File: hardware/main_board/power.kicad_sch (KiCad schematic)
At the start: 29 parts, among them J1 USB_C_Receptacle_USB2.0_16P, J2 Conn_01x03, SW1 SW_Push, U1 USBLC6-2SC6, U2 BQ24259RGER, U3 TPS7A0533PDBV

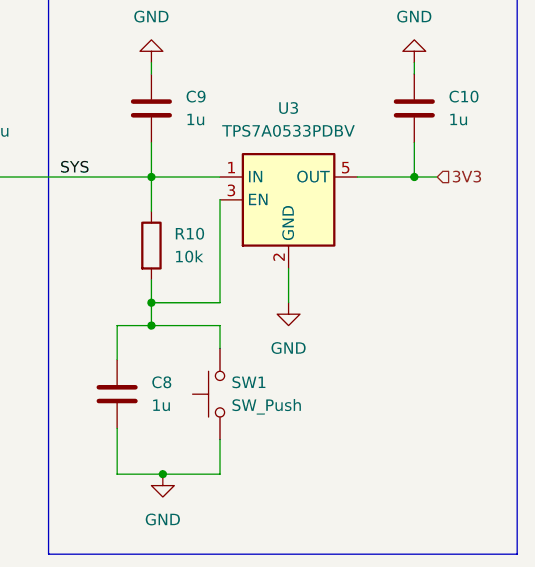
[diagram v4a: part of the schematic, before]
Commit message: Board schematic complete
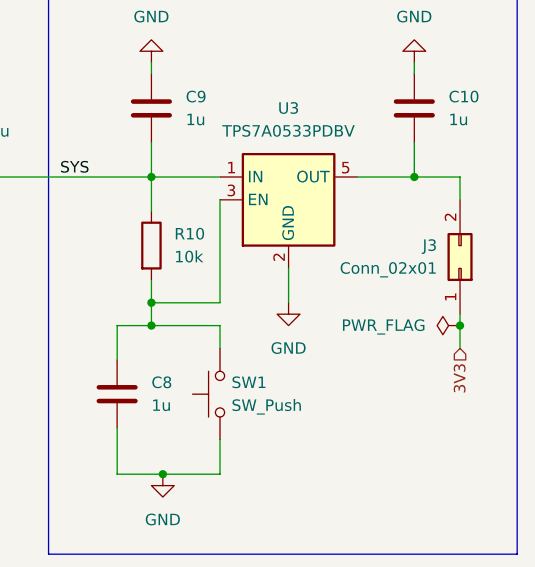
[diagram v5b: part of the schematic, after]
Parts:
- added J3: Conn_02x01, symbol Connector_Generic:Conn_02x01
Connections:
- net 3V3: now also J3.1 (Pin_1); no longer C10.2, U3.5 (OUT)
- new net: C10.2, J3.2 (Pin_2), U3.5 (OUT)
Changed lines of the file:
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@@
 	)
 	(junction
+		(at 273.05 111.76)
+		(diameter 0)
+		(color 0 0 0 0)
+	)
+	(junction
 		(at 240.03 128.27)
 		(diameter 0)
@@
 	(wire
 		(pts
-			(xy 267.97 95.25) (xy 270.51 95.25)
+			(xy 267.97 95.25) (xy 273.05 95.25)
 		)
 		(stroke
@@
 	(wire
 		(pts
+			(xy 273.05 110.49) (xy 273.05 111.76)
+		)
+		(stroke
+			(width 0)
+			(type default)
+		)
+	)
+	(wire
+		(pts
 			(xy 59.69 127) (xy 59.69 125.73)
 		)
@@
 	(wire
 		(pts
+			(xy 273.05 111.76) (xy 273.05 114.3)
+		)
+		(stroke
+			(width 0)
+			(type default)
+		)
+	)
+	(wire
+		(pts
 			(xy 59.69 90.17) (xy 74.93 90.17)
 		)
@@
 		)
 	)
+	(wire
+		(pts
+			(xy 273.05 95.25) (xy 273.05 97.79)
+		)
+		(stroke
+			(width 0)
+			(type default)
+		)
+	)
 	(rectangle
 		(start 227.33 71.12)
@@
 	(hierarchical_label "3V3"
 		(shape input)
-		(at 270.51 95.25 0)
+		(at 273.05 114.3 270)
 		(effects
 			(font
 				(size 1.27 1.27)
 			)
-			(justify left)
+			(justify right)
 		)
 	)
@@
 	)
 	(symbol
+		(lib_id "power:PWR_FLAG")
+		(at 273.05 111.76 90)
+		(unit 1)
+		(exclude_from_sim no)
+		(in_bom yes)
+		(on_board yes)
+		(dnp no)
+		(fields_autoplaced yes)
+		(property "Reference" "#FLG03"
+			(at 271.145 111.76 0)
+			(effects
+				(font
+					(size 1.27 1.27)
+				)
+				(hide yes)
+			)
+		)
+		(property "Value" "PWR_FLAG"
+			(at 269.24 111.7599 90)
+			(effects
+				(font
+					(size 1.27 1.27)
+				)
+				(justify left)
+			)
+		)
+		(property "Footprint" ""
+			(at 273.05 111.76 0)
+			(effects
+				(font
+					(size 1.27 1.27)
+				)
+				(hide yes)
+			)
+		)
+		(property "Datasheet" "~"
+			(at 273.05 111.76 0)
+			(effects
+				(font
+					(size 1.27 1.27)
+				)
+				(hide yes)
+			)
+		)
+		(property "Description" "Special symbol for telling ERC where power comes from"
+			(at 273.05 111.76 0)
+			(effects
+				(font
+					(size 1.27 1.27)
+				)
+				(hide yes)
+			)
+		)
+		(pin "1"
+		)
+		(instances
+			(project ""
+				(path "/e7586151-38a0-41a9-9cce-542cfb7665db/36d2f76b-6786-406f-96a1-52265f303dbc"
+					(reference "#FLG03")
+					(unit 1)
+				)
+			)
+		)
+	)
+	(symbol
 		(lib_id "Device:C")
 		(at 189.23 106.68 0)
@@
 					(unit 1)
 				)
+			)
+		)
+	)
+	(symbol
+		(lib_id "Connector_Generic:Conn_02x01")
+		(at 273.05 105.41 270)
+		(mirror x)
+		(unit 1)
+		(exclude_from_sim no)
+		(in_bom yes)
+		(on_board yes)
+		(dnp no)
+		(property "Reference" "J3"
+			(at 270.51 102.8699 90)
+			(effects
+				(font
+					(size 1.27 1.27)
+				)
+				(justify right)
+			)
+		)
+		(property "Value" "Conn_02x01"
+			(at 270.51 105.4099 90)
+			(effects
+				(font
+					(size 1.27 1.27)
+				)
+				(justify right)
+			)
+		)
+		(property "Footprint" ""
+			(at 273.05 105.41 0)
+			(effects
+				(font
+					(size 1.27 1.27)
+				)
+				(hide yes)
+			)
+		)
+		(property "Datasheet" "~"
+			(at 273.05 105.41 0)
+			(effects
+				(font
+					(size 1.27 1.27)
+				)
+				(hide yes)
+			)
+		)
+		(property "Description" "Generic connector, double row, 02x01, this symbol is compatible with counter-clockwise, top-bottom and odd-even numbering schemes., script generated (kicad-library-utils/schlib/autogen/connector/)"
+			(at 273.05 105.41 0)
+			(effects
+				(font
+					(size 1.27 1.27)
+				)
+				(hide yes)
+			)
+		)
+		(pin "2"
+		)
+		(pin "1"
+		)
+		(instances
+			(project ""
+				(path "/e7586151-38a0-41a9-9cce-542cfb7665db/36d2f76b-6786-406f-96a1-52265f303dbc"
+					(reference "J3")
+					(unit 1)
+				)

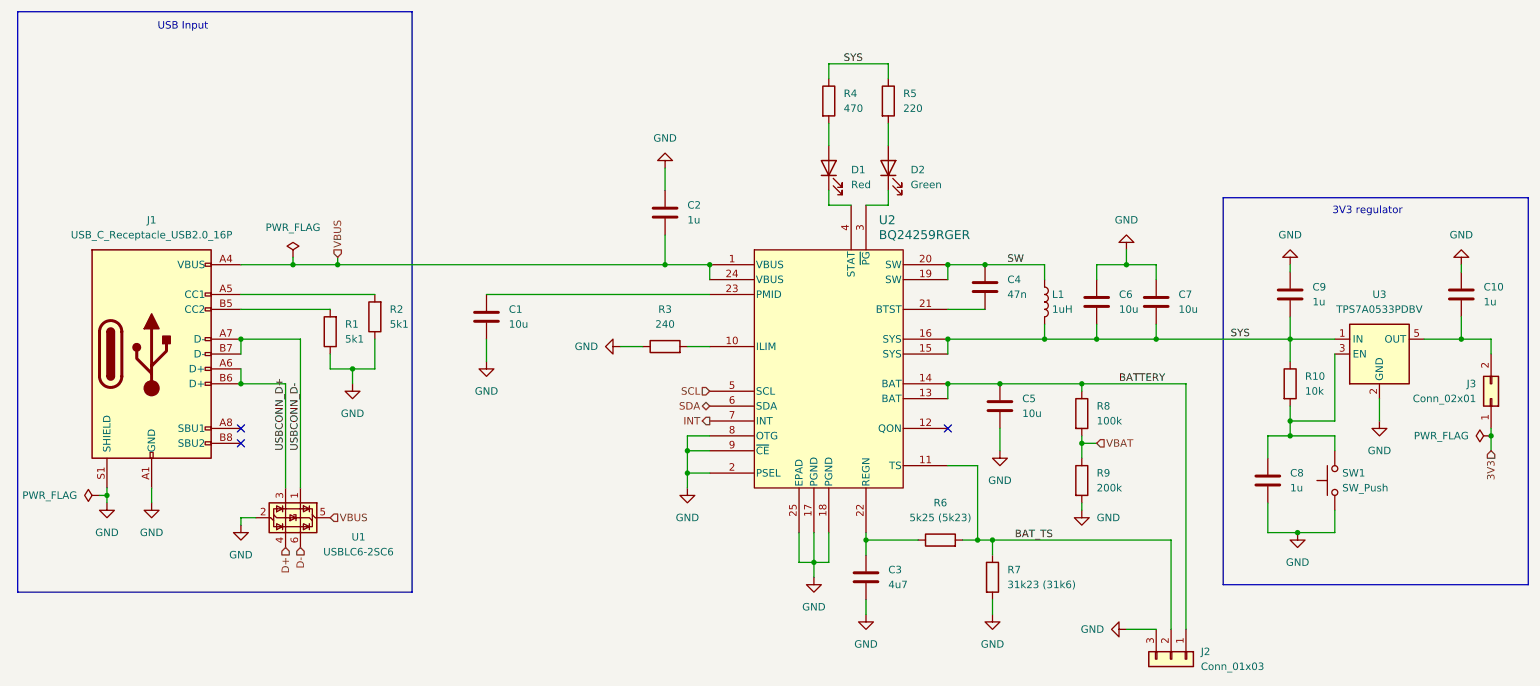
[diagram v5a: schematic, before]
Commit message: Routed mainboard PCB
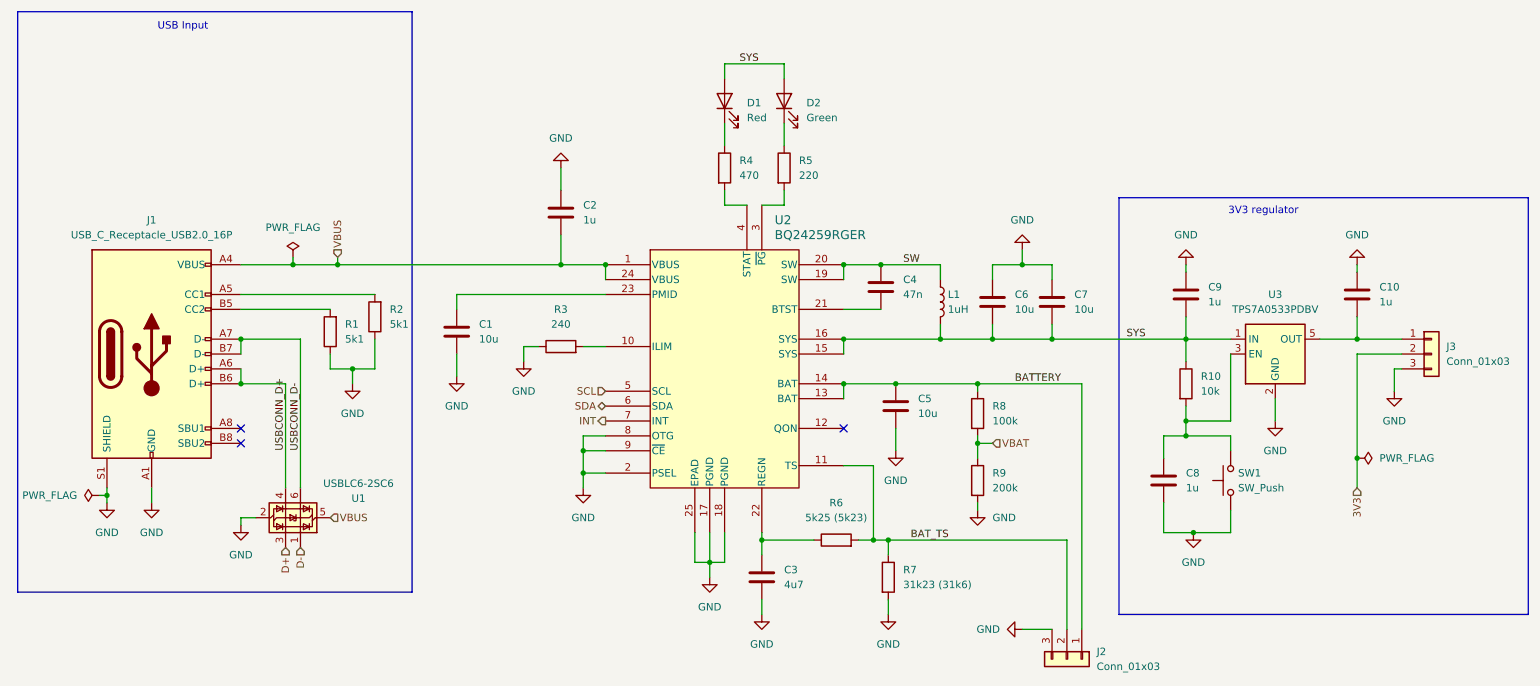
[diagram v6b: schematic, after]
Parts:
- removed J3: Conn_02x01, symbol Connector_Generic:Conn_02x01
- added J3: Conn_01x03, Connector_Harwin:Harwin_M20-89003xx_1x03_P2.54mm_Horizontal, symbol Connector_Generic:Conn_01x03
- SW1: Function (none) -> 3V3 LDO reset
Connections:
- net 3V3: now also J3.2 (Pin_2)
- net D+: now also U1.3 (I/O2); no longer U1.4 (I/O2)
- net D-: now also U1.1 (I/O1); no longer U1.6 (I/O1)
- net GND: now also J3.3 (Pin_3)
- net SYS: now also D1.2 (A), D2.2 (A); no longer R4.1, R5.1
- net USBCONN_D+: now also U1.4 (I/O2); no longer U1.3 (I/O2)
- net USBCONN_D-: now also U1.6 (I/O1); no longer U1.1 (I/O1)
- net at C10.2, U3.5 (OUT): now also J3.1 (Pin_1)
- net at U2.3 (~{PG}): now also R5.2; no longer D2.1 (K)
- net at U2.4 (STAT): now also R4.2; no longer D1.1 (K)
- new net: D2.1 (K), R5.1
- new net: D1.1 (K), R4.1
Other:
- moved on the sheet: C1, C10, C2, C3, C4, C5, C6, C7, C8, C9, D1, D2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

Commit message: Update component IDs
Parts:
- C4: JLCPCB C5142571 -> C384812
- U1: JLCPCB (none) -> C7519
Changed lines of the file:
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@@
+			)
+		)
+		(property "JLCPCB" "C7519"
+			(at 69.85 125.73 0)
+			(effects
+				(font
+					(size 1.27 1.27)
+				)
+				(hide yes)
 			)
 		)
@@
 			)
 		)
-		(property "JLCPCB" "C5142571"
+		(property "JLCPCB" "C384812"
 			(at 168.91 86.36 0)
 			(effects
